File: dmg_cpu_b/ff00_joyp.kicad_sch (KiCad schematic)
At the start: 59 parts, among them P10 IOBUF_B, P11 IOBUF_B, P12 IOBUF_B, P13 IOBUF_B, P14 OBUF_B, P15 OBUF_B

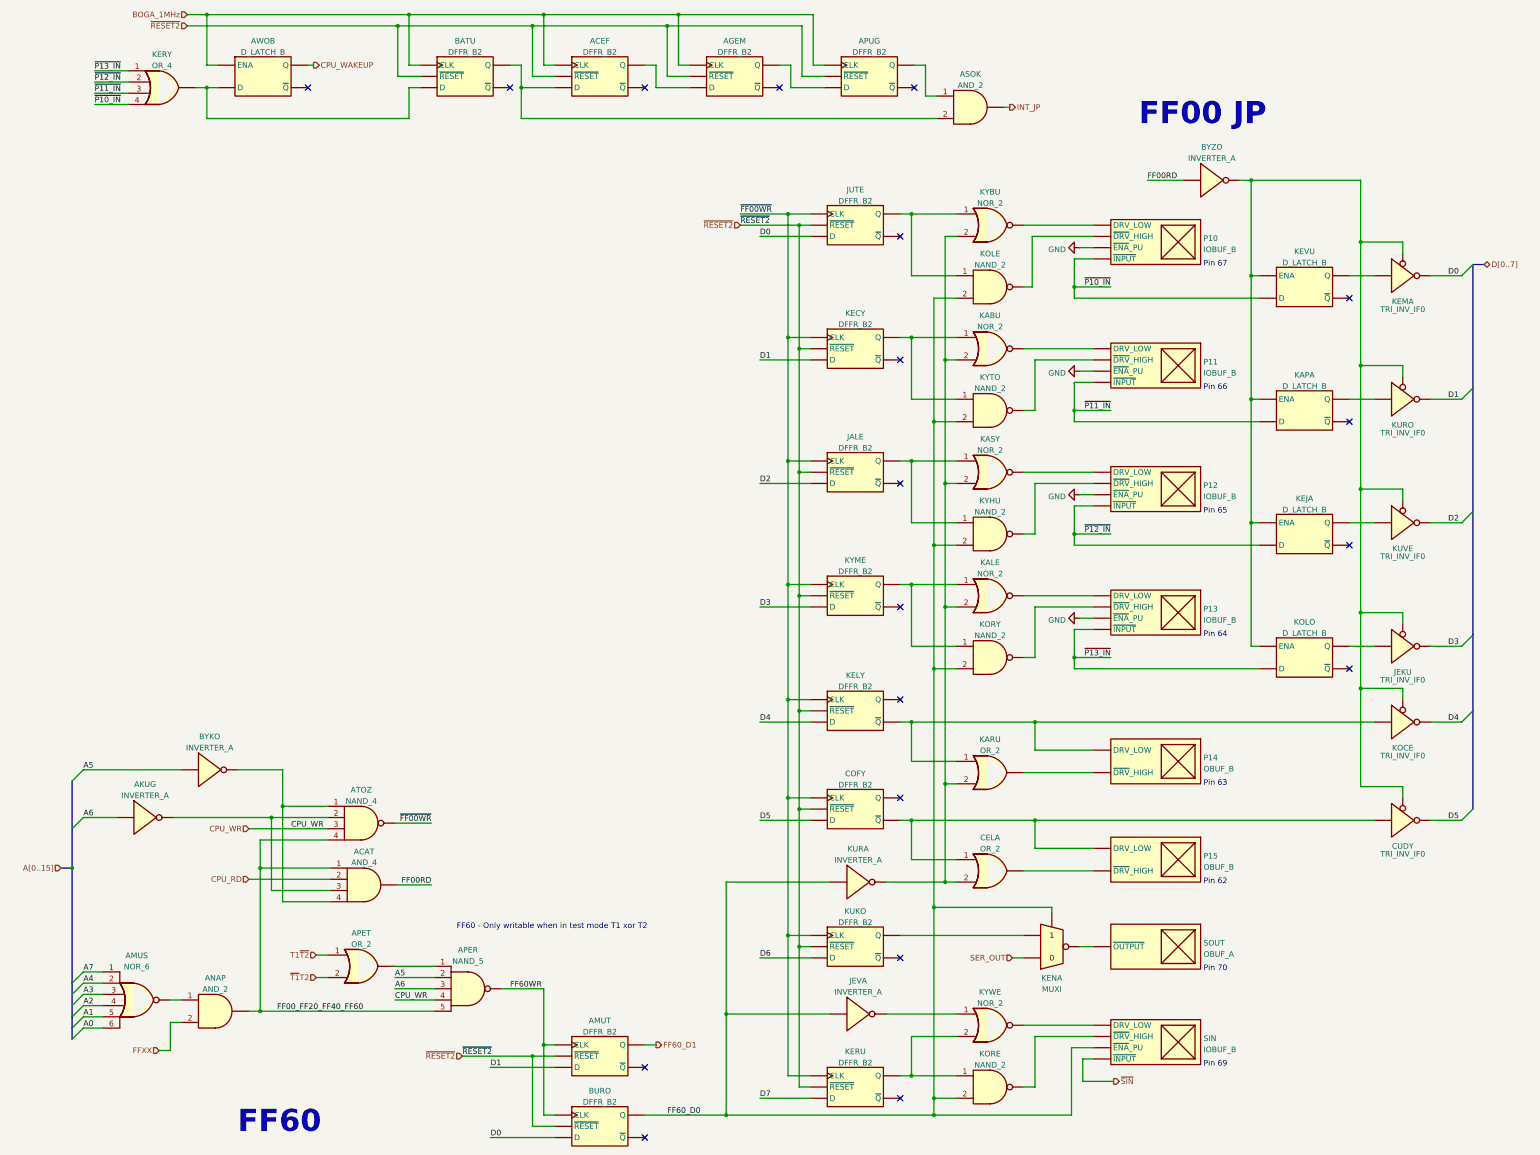
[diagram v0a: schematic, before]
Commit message: Give more meaningful names to cell types
Before this commit, many of the cells types in the chip were named in a
sloppy manner. The different inverter, latch and flip flop valiants were
just suffixed with A, B, C, D, ... Those suffixes gave no information
about the actual differences. They had to be looked up in the
documentation. Now the names of cell types with different variants have
changed:

* Inverter types are named NOT_X1, NOT_X2, NOT_X3, ... The _Xn suffix
  reflects the drive strength of the cell. X1 is the drive strength of
  the weakest inverter, X2 is double the drive strength of the weakest
  inverter.
* Flip flop types are named DFFR, DFFR_CC, DFFR_CC_Q. DFFR is a normal
  data flip flop with reset and a single clock input. The suffix _CC is
  added to flip flops that have two complementary clock inputs (CLK and
  /CLK). Flip flops that only have the positive Q output are suffixed
  with _Q.
* Latch types are named similar to flip flops: DLATCH, DLATCH_EE,
  DLATCH_EE_Q. The suffix _EE is given to latches that require
  "externally inverted enable" signals (ENA and /ENA).
* I/O pad types all start with PAD_BIDIR, PAD_IN or PAD_OUT. They also
  have suffixes that describe what makes them unique, like _PU for
  pull-ups.

Other minor changes were made to align the names with common naming
schemes of other cell libraries.
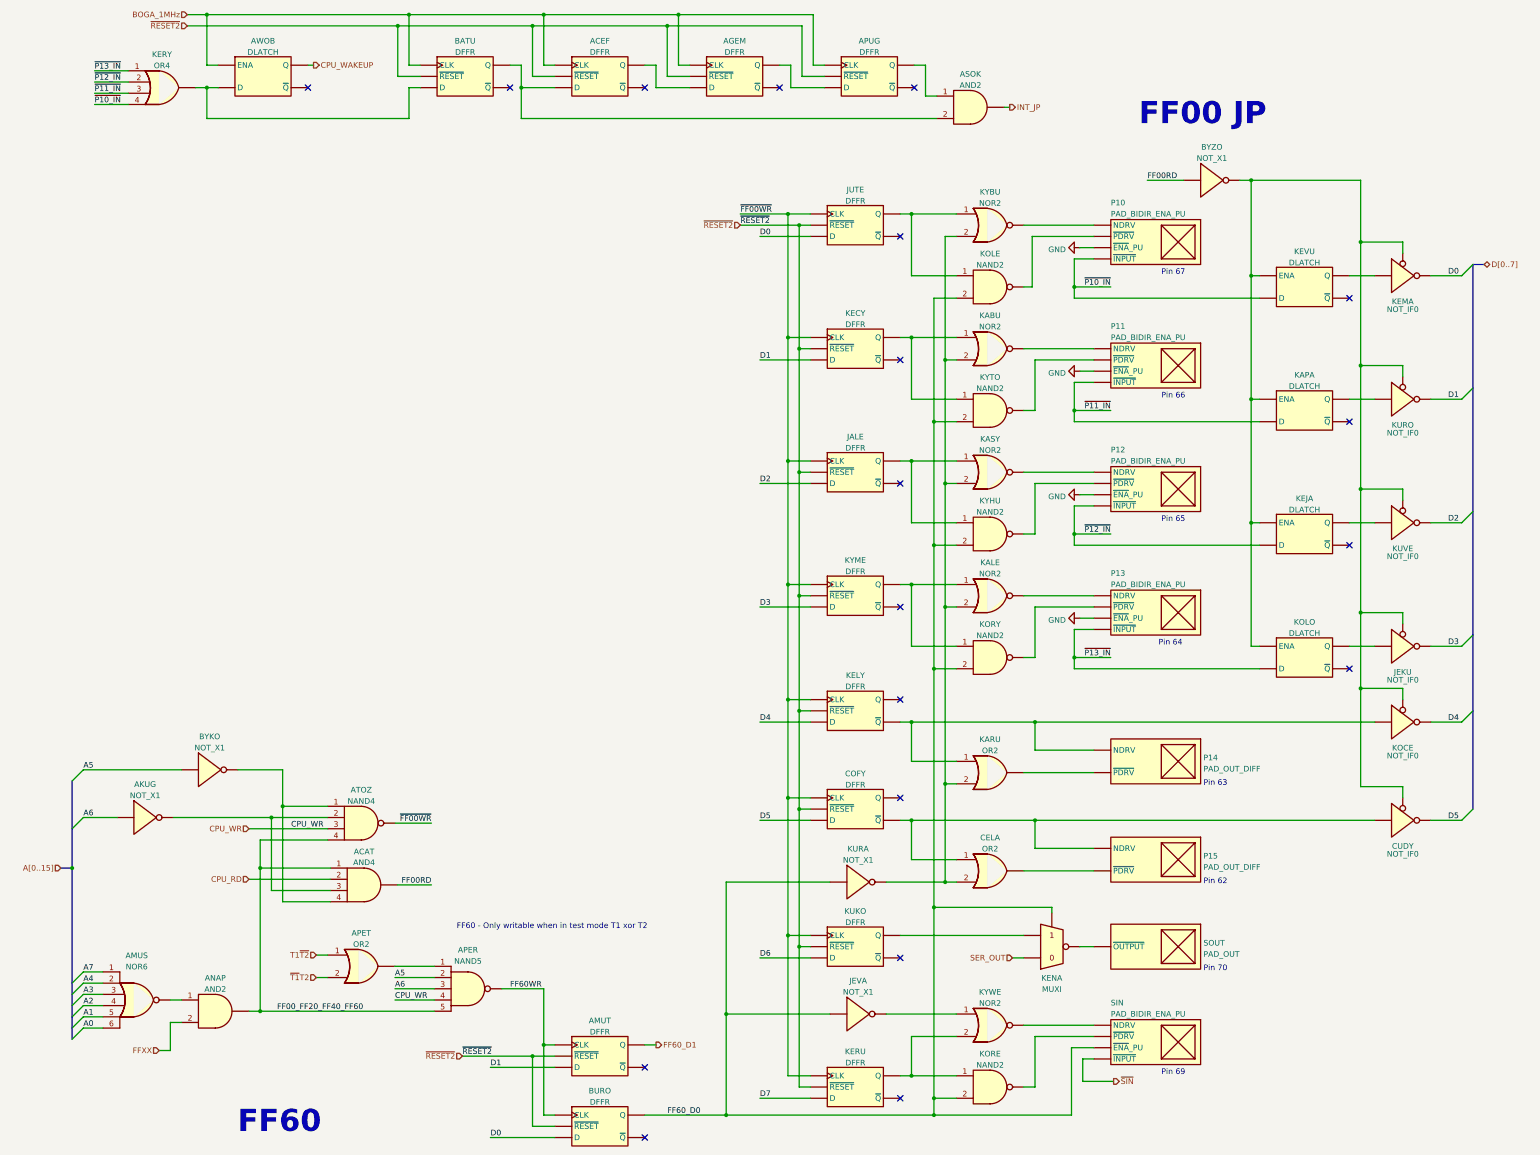
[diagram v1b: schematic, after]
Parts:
- ACAT: value AND_4 -> AND4; symbol DMG_CPU_Cells:AND_4 -> DMG_CPU_Cells:AND4
- ACEF, AGEM, AMUT, APUG, BATU, BURO, COFY, JALE, JUTE, KECY, KELY, KERU, KUKO, KYME: value DFFR_B2 -> DFFR; symbol DMG_CPU_Cells:DFFR_B2 -> DMG_CPU_Cells:DFFR
- AKUG, BYKO, BYZO, JEVA, KURA: value INVERTER_A -> NOT_X1; symbol DMG_CPU_Cells:INVERTER_A -> DMG_CPU_Cells:NOT_X1
- AMUS: value NOR_6 -> NOR6; symbol DMG_CPU_Cells:NOR_6 -> DMG_CPU_Cells:NOR6
- ANAP, ASOK: value AND_2 -> AND2; symbol DMG_CPU_Cells:AND_2 -> DMG_CPU_Cells:AND2
- APER: value NAND_5 -> NAND5; symbol DMG_CPU_Cells:NAND_5 -> DMG_CPU_Cells:NAND5
- APET, CELA, KARU: value OR_2 -> OR2; symbol DMG_CPU_Cells:OR_2 -> DMG_CPU_Cells:OR2
- ATOZ: value NAND_4 -> NAND4; symbol DMG_CPU_Cells:NAND_4 -> DMG_CPU_Cells:NAND4
- AWOB, KAPA, KEJA, KEVU, KOLO: value D_LATCH_B -> DLATCH; symbol DMG_CPU_Cells:D_LATCH_B -> DMG_CPU_Cells:DLATCH
- CUDY, JEKU, KEMA, KOCE, KURO, KUVE: value TRI_INV_IF0 -> NOT_IF0; symbol DMG_CPU_Cells:TRI_INV_IF0 -> DMG_CPU_Cells:NOT_IF0
- KABU, KALE, KASY, KYBU, KYWE: value NOR_2 -> NOR2; symbol DMG_CPU_Cells:NOR_2 -> DMG_CPU_Cells:NOR2
- KERY: value OR_4 -> OR4; symbol DMG_CPU_Cells:OR_4 -> DMG_CPU_Cells:OR4
- KOLE, KORE, KORY, KYHU, KYTO: value NAND_2 -> NAND2; symbol DMG_CPU_Cells:NAND_2 -> DMG_CPU_Cells:NAND2
- P10, P11, P12, P13, SIN: value IOBUF_B -> PAD_BIDIR_ENA_PU; symbol DMG_CPU_Cells:IOBUF_B -> DMG_CPU_Cells:PAD_BIDIR_ENA_PU
- P14, P15: value OBUF_B -> PAD_OUT_DIFF; symbol DMG_CPU_Cells:OBUF_B -> DMG_CPU_Cells:PAD_OUT_DIFF
- SOUT: value OBUF_A -> PAD_OUT; symbol DMG_CPU_Cells:OBUF_A -> DMG_CPU_Cells:PAD_OUT

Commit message: SM83 Layout: Add bottom part of sequencer cells
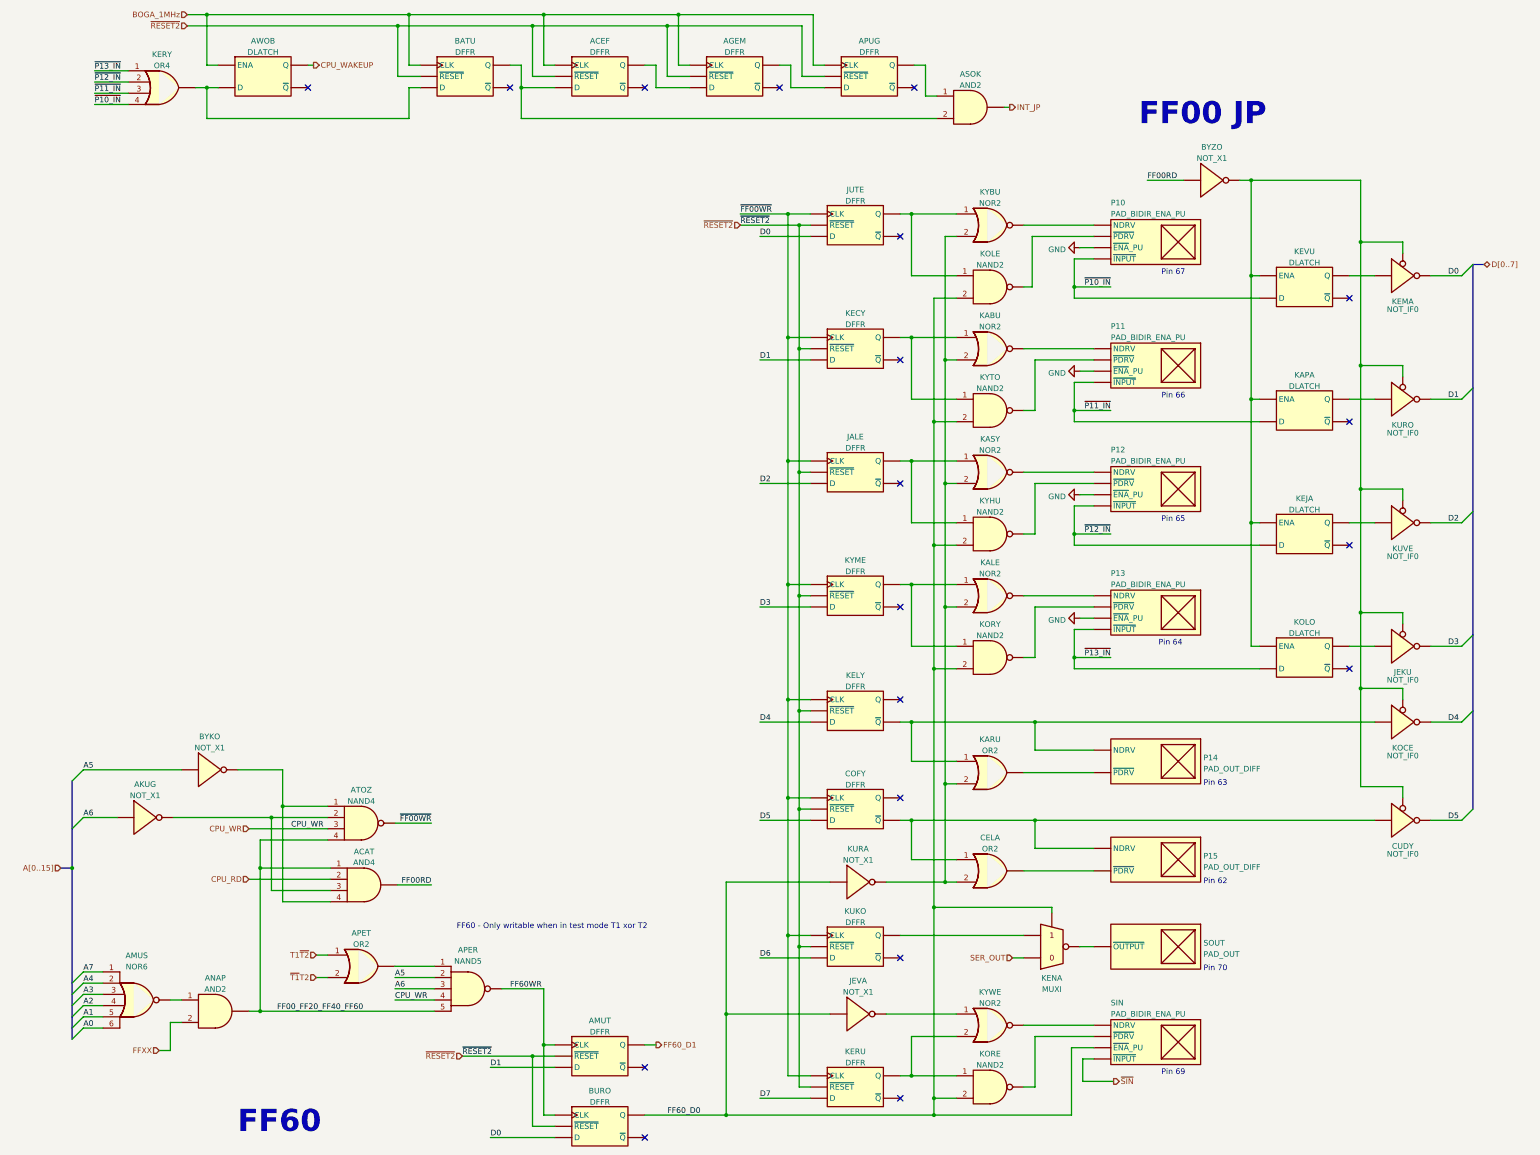
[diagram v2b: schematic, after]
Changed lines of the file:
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@@
 (kicad_sch
-	(version 20231120)
+	(version 20250114)
 	(generator "eeschema")
-	(generator_version "8.0")
+	(generator_version "9.0")
 	(paper "A3")
 	(title_block
 		(title "DMG-CPU B")
-		(date "2025-04-12")
+		(date "2025-04-22")
 		(rev "0.7")
 		(company "CC-BY-SA-4.0 Régis Galland & Michael Singer -- Derived work from Furrtek")
 		(comment 1 "https://github.com/msinger/dmg-schematics")
 	)
+	(text "Pin 66"
+		(exclude_from_sim no)
+		(at 278.765 108.585 0)
+		(effects
+			(font
+				(size 1.27 1.27)
+			)
+			(justify left bottom)
+		)
+	)
+	(text "FF60 - Only writable when in test mode T1 xor T2"
+		(exclude_from_sim no)
+		(at 119.38 228.6 0)
+		(effects
+			(font
+				(size 1.27 1.27)
+			)
+			(justify left bottom)
+		)
+	)
+	(text "Pin 70"
+		(exclude_from_sim no)
+		(at 288.29 238.125 0)
+		(effects
+			(font
+				(size 1.27 1.27)
+			)
+			(justify left bottom)
+		)
+	)
+	(text "Pin 62"
+		(exclude_from_sim no)
+		(at 288.29 218.44 0)
+		(effects
+			(font
+				(size 1.27 1.27)
+			)
+			(justify left bottom)
+		)
+	)
+	(text "Pin 64"
+		(exclude_from_sim no)
+		(at 278.13 164.465 0)
+		(effects
+			(font
+				(size 1.27 1.27)
+			)
+			(justify left bottom)
+		)
+	)
+	(text "Pin 67"
+		(exclude_from_sim no)
+		(at 278.765 80.645 0)
+		(effects
+			(font
+				(size 1.27 1.27)
+			)
+			(justify left bottom)
+		)
+	)
+	(text "Pin 63"
+		(exclude_from_sim no)
+		(at 288.29 196.215 0)
+		(effects
+			(font
+				(size 1.27 1.27)
+			)
+			(justify left bottom)
+		)
+	)
+	(text "FF60\n"
+		(exclude_from_sim no)
+		(at 69.85 274.955 0)
+		(effects
+			(font
+				(size 5 5)
+				(thickness 1)
+				(bold yes)
+			)
+			(justify left bottom)
+		)
+	)
+	(text "FF00 JP\n"
+		(exclude_from_sim no)
+		(at 273.685 46.99 0)
+		(effects
+			(font
+				(size 5 5)
+				(thickness 1)
+				(bold yes)
+			)
+			(justify left bottom)
+		)
+	)
+	(text "Pin 65"
+		(exclude_from_sim no)
+		(at 278.765 136.525 0)
+		(effects
+			(font
+				(size 1.27 1.27)
+			)
+			(justify left bottom)
+		)
+	)
+	(text "Pin 69"
+		(exclude_from_sim no)
+		(at 278.765 261.62 0)
+		(effects
+			(font
+				(size 1.27 1.27)
+			)
+			(justify left bottom)
+		)
+	)
 	(junction
 		(at 259.08 111.125)
@@
 		)
 	)
-	(text "Pin 66"
-		(exclude_from_sim no)
-		(at 278.765 108.585 0)
-		(effects
-			(font
-				(size 1.27 1.27)
-			)
-			(justify left bottom)
-		)
-	)
-	(text "FF60 - Only writable when in test mode T1 xor T2"
-		(exclude_from_sim no)
-		(at 119.38 228.6 0)
-		(effects
-			(font
-				(size 1.27 1.27)
-			)
-			(justify left bottom)
-		)
-	)
-	(text "Pin 70"
-		(exclude_from_sim no)
-		(at 288.29 238.125 0)
-		(effects
-			(font
-				(size 1.27 1.27)
-			)
-			(justify left bottom)
-		)
-	)
-	(text "Pin 62"
-		(exclude_from_sim no)
-		(at 288.29 218.44 0)
-		(effects
-			(font
-				(size 1.27 1.27)
-			)
-			(justify left bottom)
-		)
-	)
-	(text "Pin 64"
-		(exclude_from_sim no)
-		(at 278.13 164.465 0)
-		(effects
-			(font
-				(size 1.27 1.27)
-			)
-			(justify left bottom)
-		)
-	)
-	(text "Pin 67"
-		(exclude_from_sim no)
-		(at 278.765 80.645 0)
-		(effects
-			(font
-				(size 1.27 1.27)
-			)
-			(justify left bottom)
-		)
-	)
-	(text "Pin 63"
-		(exclude_from_sim no)
-		(at 288.29 196.215 0)
-		(effects
-			(font
-				(size 1.27 1.27)
-			)
-			(justify left bottom)
-		)
-	)
-	(text "FF60\n"
-		(exclude_from_sim no)
-		(at 69.85 274.955 0)
-		(effects
-			(font
-				(size 5 5)
-				(thickness 1)
-				(bold yes)
-			)
-			(justify left bottom)
-		)
-	)
-	(text "FF00 JP\n"
-		(exclude_from_sim no)
-		(at 273.685 46.99 0)
-		(effects
-			(font
-				(size 5 5)
-				(thickness 1)
-				(bold yes)
-			)
-			(justify left bottom)
-		)
-	)
-	(text "Pin 65"
-		(exclude_from_sim no)
-		(at 278.765 136.525 0)
-		(effects
-			(font
-				(size 1.27 1.27)
-			)
-			(justify left bottom)
-		)
-	)
-	(text "Pin 69"
-		(exclude_from_sim no)
-		(at 278.765 261.62 0)
-		(effects
-			(font
-				(size 1.27 1.27)
-			)
-			(justify left bottom)
-		)
-	)

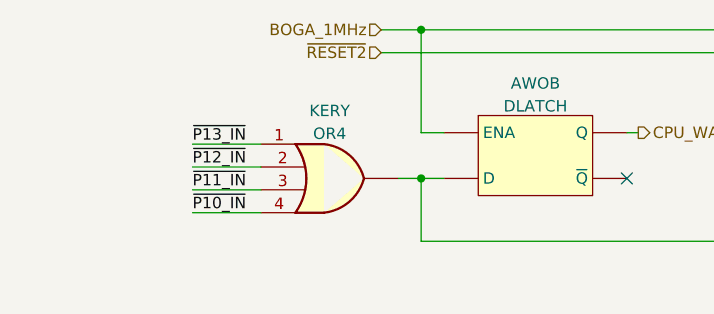
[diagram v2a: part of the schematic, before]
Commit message: DMG: Update CPU symbol and port names in schematic
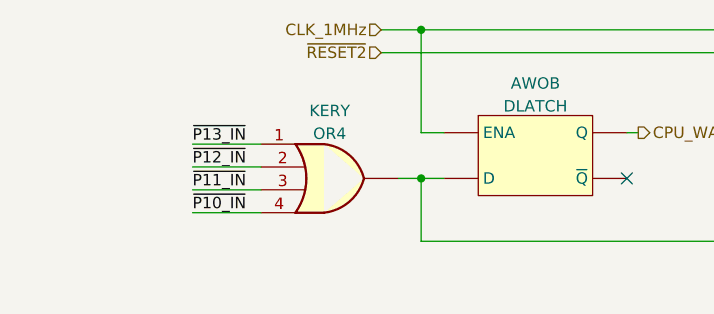
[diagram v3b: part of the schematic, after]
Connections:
- net BOGA_1MHz renamed CLK_1MHz
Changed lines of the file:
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@@
 	(title_block
 		(title "DMG-CPU B")
-		(date "2025-04-22")
-		(rev "0.7")
+		(date "2025-11-28")
+		(rev "0.8")
 		(company "CC-BY-SA-4.0 Régis Galland & Michael Singer -- Derived work from Furrtek")
 		(comment 1 "https://github.com/msinger/dmg-schematics")
@@
 		)
 	)
-	(hierarchical_label "BOGA_1MHz"
+	(hierarchical_label "CLK_1MHz"
 		(shape input)
 		(at 58.42 21.59 180)
